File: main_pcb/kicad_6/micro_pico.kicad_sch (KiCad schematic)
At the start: 18 parts, among them J101 PJ301M-12, J102 PJ301M-12, J103 PJ301M-12, J104 PJ301M-12, J105 PJ301M-12, J106 PJ301M-12, J107 PJ-011A, P101 VCF_plug_in_port, SW101 SW_SPDT_CO

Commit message: Update rev 0.1, fix VCA tails, add local 2v5 regs, change some pot footprints
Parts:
- removed TP109: VCA_AM_CV, TestPoint:TestPoint_Keystone_5000-5004_Miniature, symbol Connector:TestPoint
- R101: value 1k -> 10k
- RV101: value 100k -> 10k
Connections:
- net +2V5_REF renamed +5V

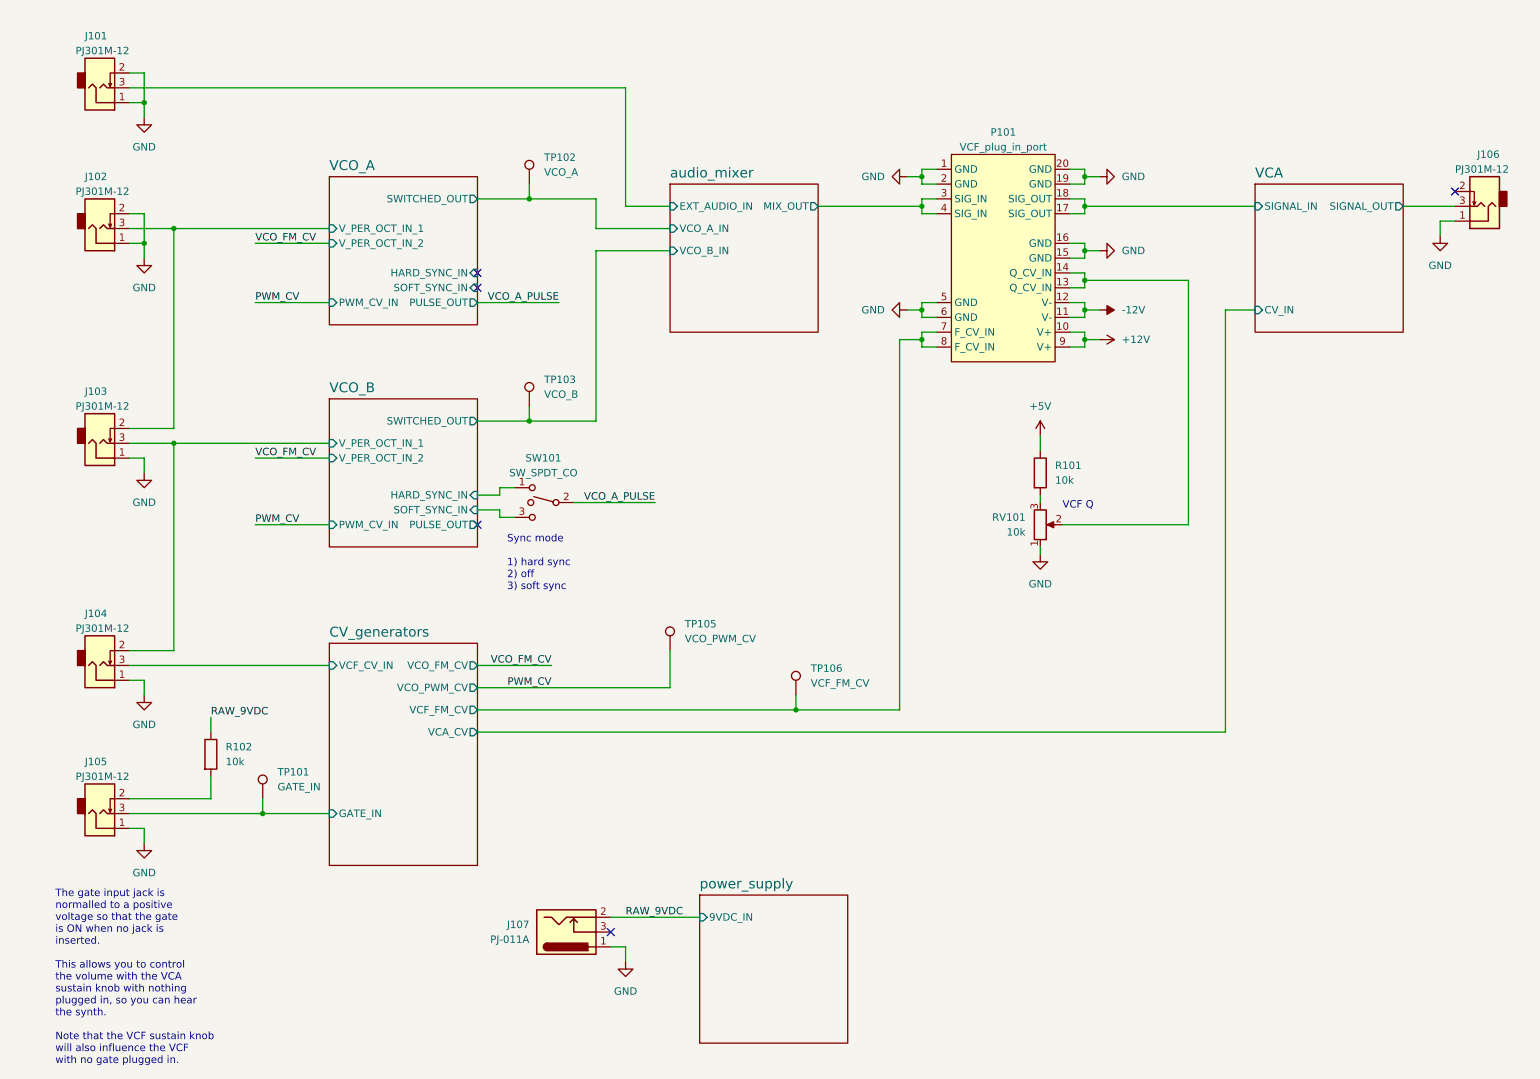
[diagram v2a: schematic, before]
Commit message: Add mod-wheel VCA, fix occasional VCO freq locking
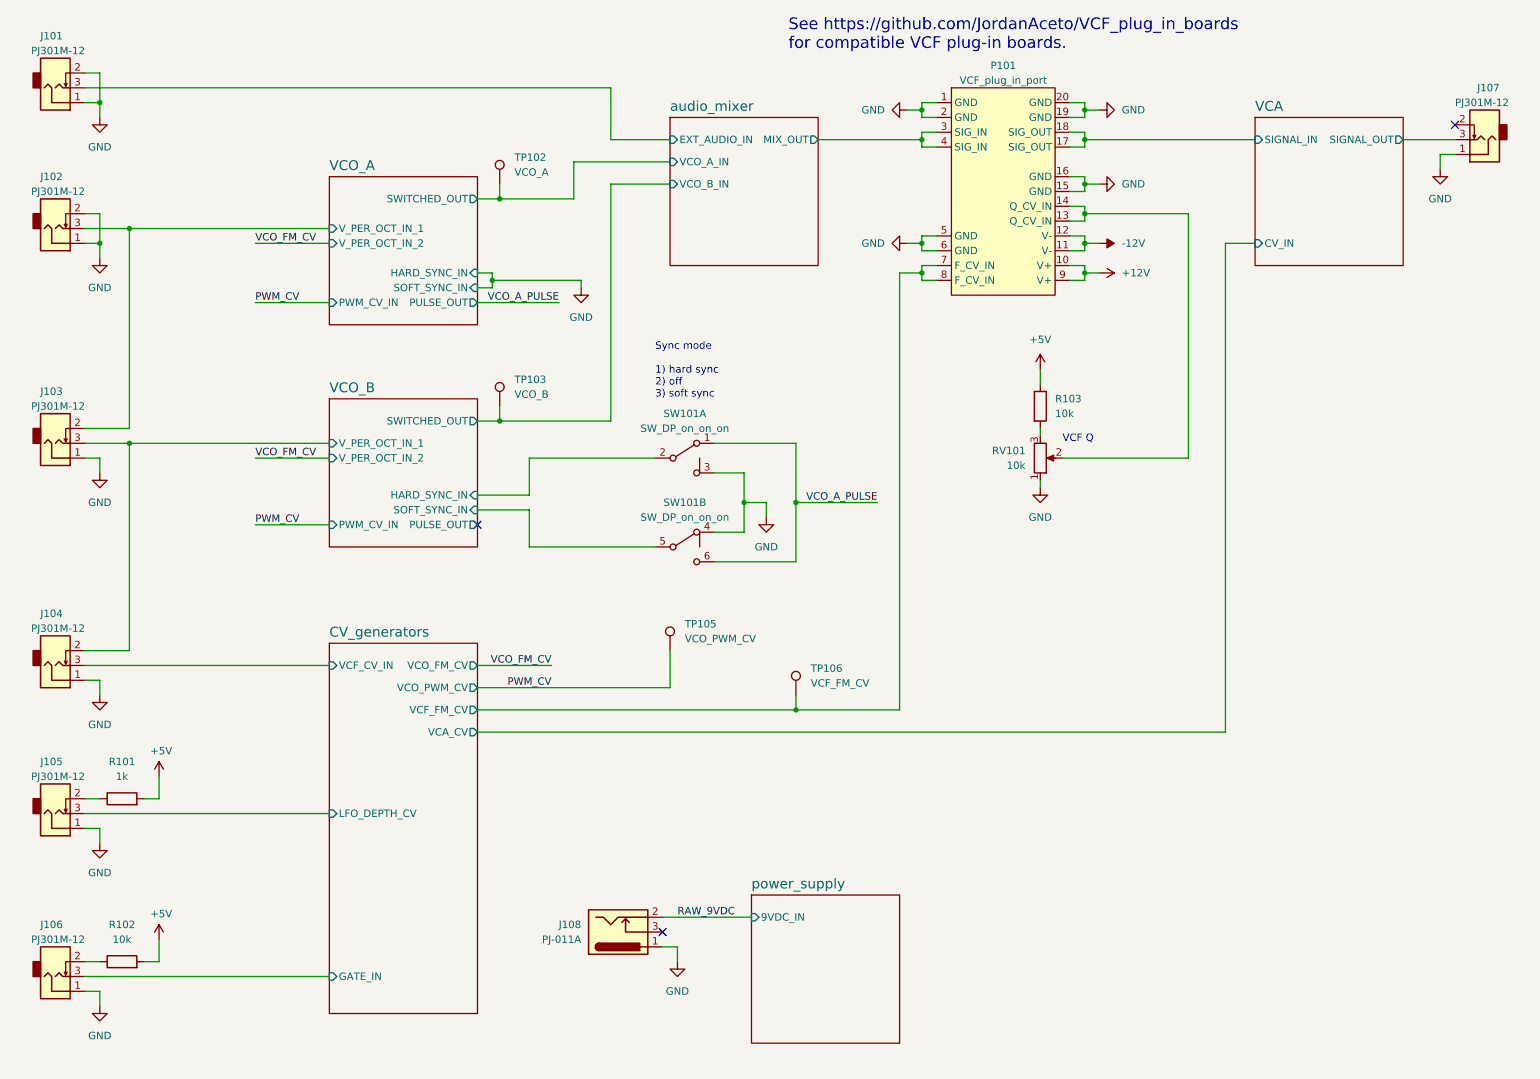
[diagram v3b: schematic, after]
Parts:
- removed SW101: SW_SPDT_CO, custom_footprints:SPDT_mini_toggle, symbol Switch:SW_SPDT_MSM
- removed TP101: GATE_IN, TestPoint:TestPoint_Keystone_5000-5004_Miniature, symbol Connector:TestPoint
- added J105: PJ301M-12, custom_footprints:PJ301M-12, symbol custom_symbols:PJ301M-12
- added R101: 1k, Resistor_SMD:R_0603_1608Metric, symbol Device:R
- added SW101: SW_DP_on_on_on, custom_footprints:DPDT_mini_toggle, symbol custom_symbols:SW_DP_on_on_on
- renumbered J105 to J106, J106 to J107, J107 to J108, R101 to R103
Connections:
- net +5V: now also R102.2, R101.2
- net GND: now also J105.1, SW101.3 (C), SW101.4 (A)
- net RAW_9VDC: no longer R102.1
- net VCO_A_PULSE: now also SW101.1 (A), SW101.6 (C)
- net VCO_B/HARD_SYNC_IN: now also SW101.2 (B)
- net VCO_B/SOFT_SYNC_IN: now also SW101.5 (B)
- net at J106.2: now also R102.1; no longer R102.2
- new net: J105.2, R101.1
- new net CV_generators/LFO_DEPTH_CV: J105.3
- no-connect marks 5 -> 3
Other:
- sheet CV_generators ports: added LFO_DEPTH_CV; removed none
- note added: "See https://github.com/JordanAceto/VCF_plug_in_boards for compatible VCF plug-in boards."
- note removed: "The gate input jack is normalled to a positive voltage so that the gate is ON when no jack is inserted. This allows you to control the volume with the VCA sustain knob with nothing plugged in, so you can hear the synth. Note that the VCF sustain knob will also influence the VCF with no gate plugged in."
- moved on the sheet: J101, J102, J103, J104, J106, J107, J108, P101, R102, R103, RV101, TP102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
